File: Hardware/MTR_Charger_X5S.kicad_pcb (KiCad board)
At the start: 2 copper layers, 122 parts, among them J1 Korean Hroparts Elec TYPE-C-3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, J2 Micro_SD_Card, Q1 IRF7324TRPBF, Q10 AO3480C, Q11 AO3480C, Q2 AO3401A, Q3 AO3401A, Q4 AO3480C, Q5 AO3480C, Q6 AO3401A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

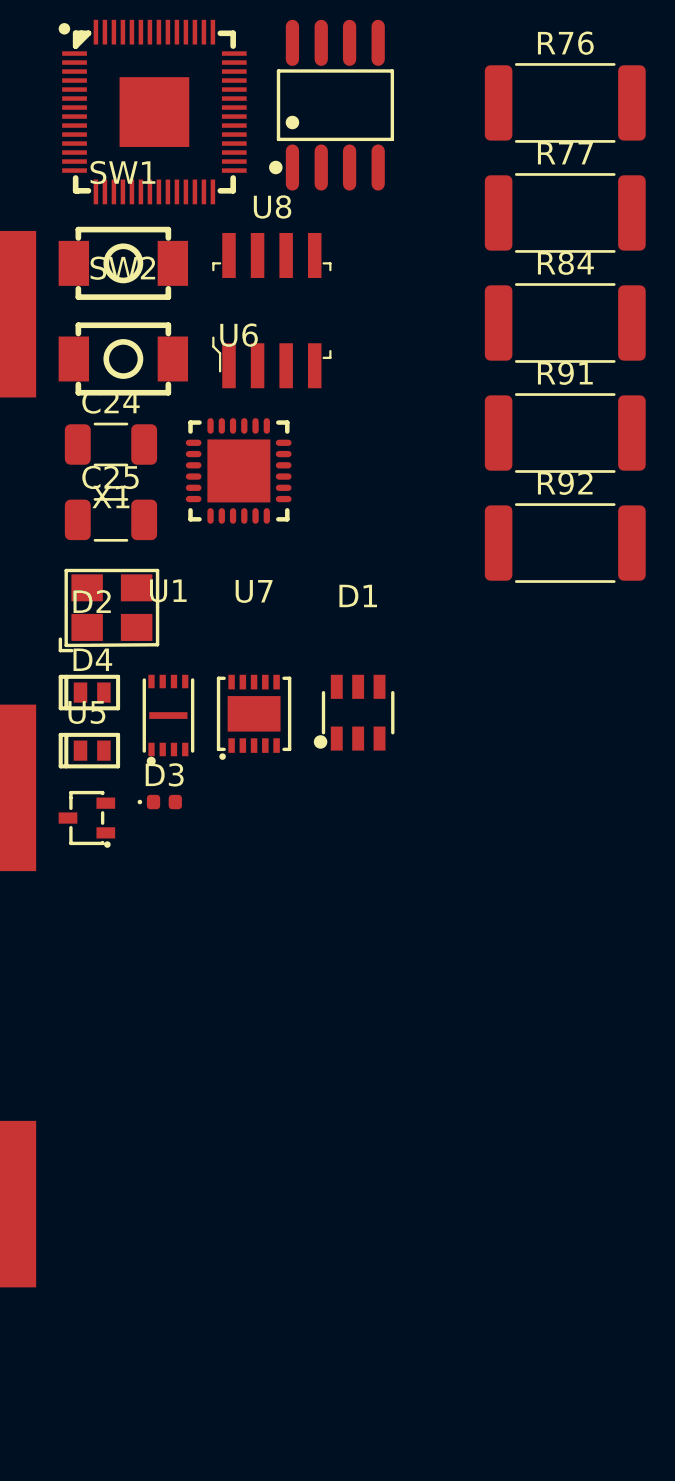
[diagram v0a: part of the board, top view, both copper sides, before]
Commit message: Add Mux for Battery charging current selection
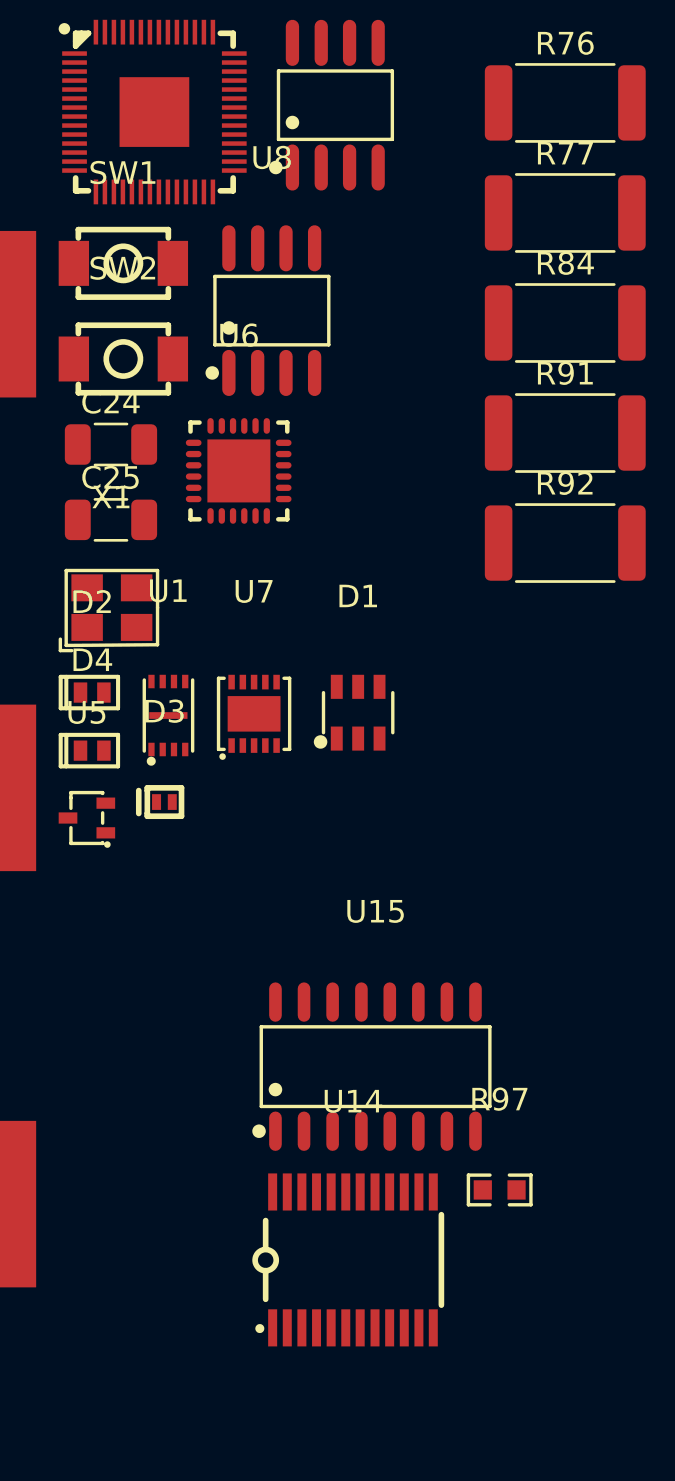
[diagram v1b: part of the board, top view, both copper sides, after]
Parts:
- added R97: NCP18XH103F03RB, easyeda2kicad:R0603, F.Cu at (149.2, 128.1)
- added U14: TCA9535PWR_C130204, easyeda2kicad:TSSOP-24_L7.8-W4.4-P0.65-LS6.4-BL, F.Cu at (142.7, 131.2)
- added U15: CD74HCT4051M96, easyeda2kicad:SOP-16_L10.0-W3.9-P1.27-LS6.0-BL, F.Cu at (143.7, 122.6)
- D3: footprint Diode_SMD:D_0402_1005Metric -> easyeda2kicad:X2-DFN1006-2_L1.0-W0.6-P0.65-RD
- U8: footprint digikey-footprints:SOIC-8_W3.9mm -> easyeda2kicad:SOIC-8_L4.9-W3.9-P1.27-LS6.0-BL
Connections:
- U7 pad 3: unconnected-(U7-STAT1-Pad3) -> /STAT1_Cell_01
- U7 pad 4: unconnected-(U7-STAT2-Pad4) -> /STAT2_Cell_01
- U7 pad 6: unconnected-(U7-PROG-Pad6) -> /PROG_CELL_01
- U7 pad 7: unconnected-(U7-~{PG}-Pad7) -> /PG_Cell_01
- U7 pad 8: unconnected-(U7-THERM-Pad8) -> Net-(U7-THERM)

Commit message: --------------
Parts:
- moved J2 1.43 mm to (137.4, 49.0)
